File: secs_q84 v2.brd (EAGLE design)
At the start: 97.5 x 69.8 mm, 107 parts, among them IC1 MAX203ECWP, IC2 REF3440TIDBVR, IC3 ADP151AUJZ-3.3-R7, IC5 MCZ33996EK, IC6 74HC125D, IC7 TIC12400DCPR, IC8 PIC18F57Q84-I_PT

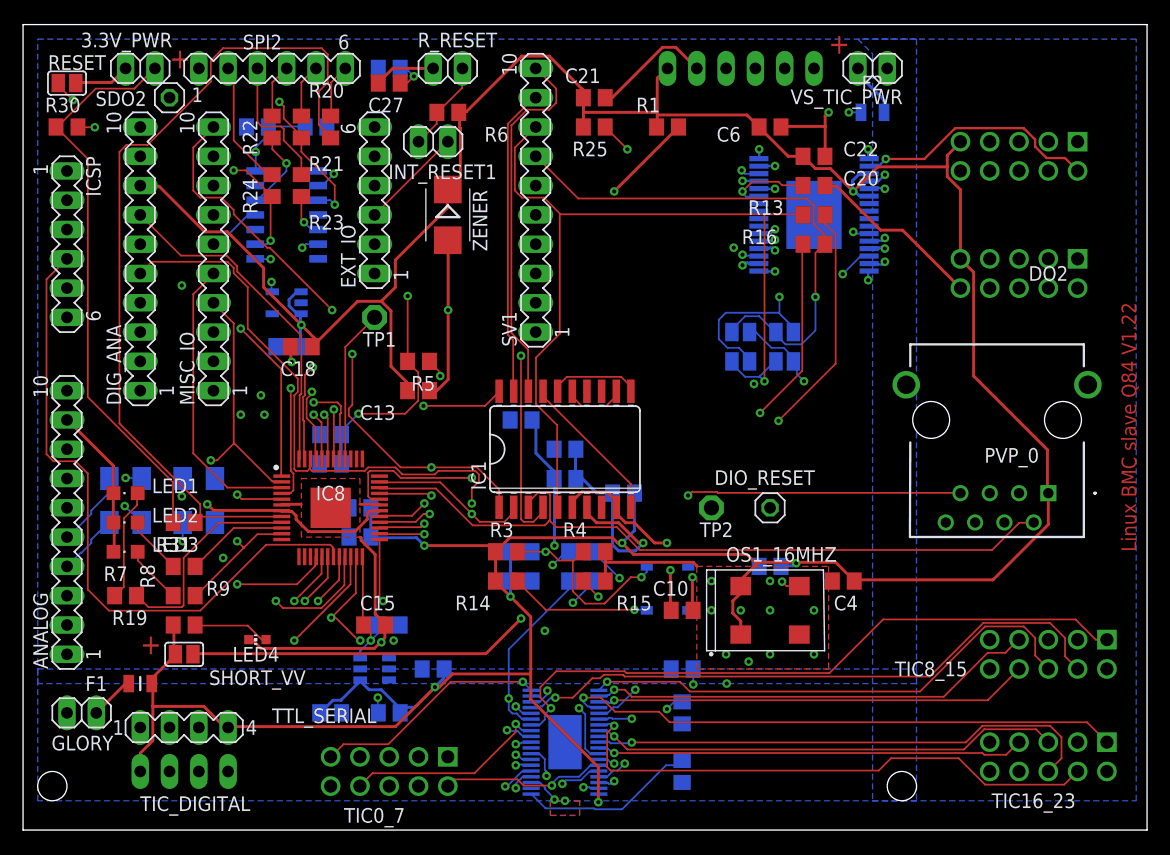
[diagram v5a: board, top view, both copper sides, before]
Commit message: 57Q84 support
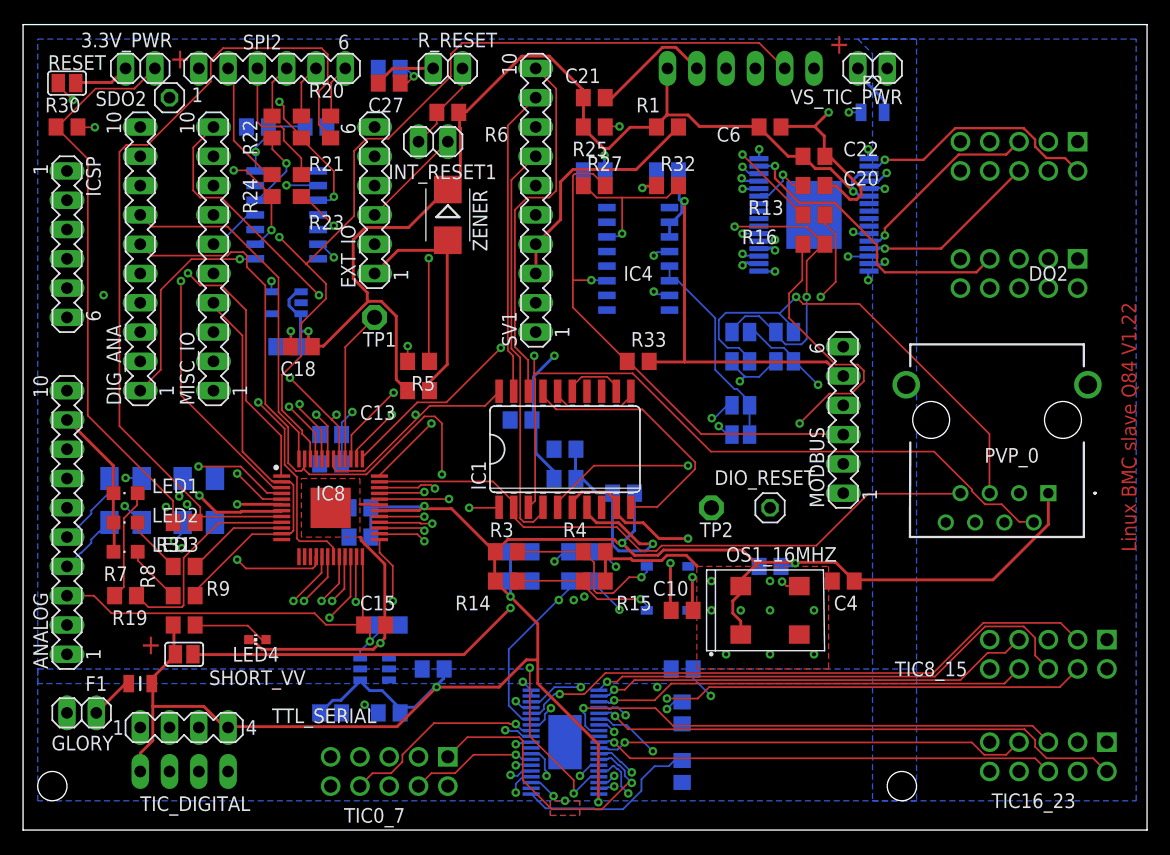
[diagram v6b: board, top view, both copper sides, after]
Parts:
- added C30: 10uf, rcl:C0805
- added C31: 0.1uf, rcl:C0805
- added DE3: DE3, jumper:SJ
- added IC4: ADM3095EBRZ, ADM3095EBRZ:SOIC127P600X175-16N
- added MODBUS: MODBUS, con-lstb:MA06-1
- added R27: 120, rcl:R0805
- added R32, R33: 1.2k, rcl:R0805
- added TXDE3: TXDE3, jumper:SJ
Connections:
- new net DE3: DE3.2, IC8.39, MODBUS.6
- new net DERE: DE3.1, IC4.5, IC4.6, TXDE3.1
- new net MB_A: IC4.11, MODBUS.3, R27.2, R33.1
- new net MB_B: IC4.14, MODBUS.2, R27.1, R32.2
- new net MOD_RX: IC4.7, IC8.36
- new net MOD_TX: IC4.4, IC8.37
- new net TXD3: IC8.38, TXDE3.2
- net VDD: now also C30.1, C31.1, IC4.2, IC4.3, MODBUS.5, R33.2
- net VSS: now also C30.2, C31.2, IC4.1, IC4.10, IC4.12, IC4.13, IC4.15, IC4.16, IC4.8, IC4.9, MODBUS.1, MODBUS.4, R32.1
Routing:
- net DE3: track 0.00 -> 52.3 mm, vias 0 -> 2
- net VDD: track 399.9 -> 448.0 mm, vias 9 -> 11
- net MB_A: track 0.00 -> 45.7 mm, vias 0 -> 1
- net MB_B: track 0.00 -> 41.7 mm, vias 0 -> 1
- net MOD_RX: track 0.00 -> 40.1 mm, vias 0 -> 2
- net TXD3: track 0.00 -> 36.1 mm, vias 0 -> 2
- net SDI1: track 138.8 -> 174.6 mm
- net MOD_TX: track 0.00 -> 34.2 mm, vias 0 -> 2
- net SDO2: track 86.9 -> 58.4 mm, vias 2 -> 3
- net MCZ_CS: track 79.3 -> 107.1 mm, vias 4 -> 2
- net TIC9: track 85.5 -> 65.8 mm, vias 1 -> 2
- net PGC_TICINT: track 110.9 -> 129.3 mm
- net SCK1: track 164.1 -> 145.9 mm, vias 3 -> 5
- net DERE: track 0.00 -> 18.1 mm
- net MB_RX: track 65.3 -> 82.3 mm, vias 0 -> 2
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
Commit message: up
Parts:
- added AUX_IO: AUX_IO, con-lstb:MA06-1
- moved C11 5.68 mm to (53.3, 33.0)
- moved F2 4.02 mm to (94.0, 76.2)
- moved VS_TIC_PWR 3.81 mm to (99.1, 76.2)
- moved C15 2.84 mm to (53.3, 30.5), flipped to the bottom, turned to 180 degrees
- moved C3 2.54 mm to (53.3, 35.6)
- moved DO1 2.54 mm to (115.6, 69.8)
- moved DO2 2.54 mm to (115.6, 59.7)
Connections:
- new net RF4: AUX_IO.3, IC8.12
- new net RF5: AUX_IO.4, IC8.13
- new net RF6: AUX_IO.5, IC8.14
- new net RF7: AUX_IO.6, IC8.15
- net VDD: now also AUX_IO.2
- net VSS: now also AUX_IO.1
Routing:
- net RF6: track 0.00 -> 120.9 mm, vias 0 -> 2
- net RF4: track 0.00 -> 105.2 mm, vias 0 -> 2
- net RF7: track 0.00 -> 103.4 mm, vias 0 -> 2
- net RF5: track 0.00 -> 99.2 mm
- net SDO2: track 58.4 -> 91.5 mm, vias 3 -> 2
- net VDD: track 448.0 -> 478.3 mm
- net SDO1: track 149.1 -> 178.6 mm
- net DIO_RST: track 62.0 -> 89.2 mm
- net SCK1: track 145.9 -> 170.6 mm, vias 5 -> 4
- net VCC: track 72.3 -> 96.6 mm
- net SDI1: track 174.6 -> 151.4 mm
- net CLOCKO: track 45.7 -> 65.2 mm, vias 2 -> 0
- net DE3: track 52.3 -> 68.8 mm
- net MB_RX: track 82.3 -> 66.1 mm
- net MCZ_CS: track 107.1 -> 91.9 mm, vias 2 -> 3
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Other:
- board text added: "Linux BMC slave Q84 V1.223"
- board text removed: "Linux BMC slave Q84 V1.22"

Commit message: up
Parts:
- added C32, C33, C34, C35: 0.1uf, rcl:C0603
- added GLORY_24: GLORY_24, pinhead:1X02
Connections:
- net RF4: now also C35.1
- net RF5: now also C32.1
- net RF6: now also C33.1
- net RF7: now also C34.1
- net VSS: now also C32.2, C33.2, C34.2, C35.2
- net VS_TIC_24V: now also GLORY_24.1, GLORY_24.2
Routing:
- net VS_TIC_24V: track 168.3 -> 176.6 mm
- net RF4: track 105.2 -> 110.9 mm, vias 2 -> 3
- net RF5: track 99.2 -> 103.4 mm
- net RF6: track 120.9 -> 124.2 mm
- net RF7: track 103.4 -> 106.1 mm
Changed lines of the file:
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@@
 <param name="RoutingGrid" value="3mil"/>
 <param name="AutoGrid" value="1"/>
-<param name="Efforts" value="2"/>
+<param name="Efforts" value="1"/>
 <param name="TopRouterVariant" value="1"/>
 <param name="tpViaShape" value="round"/>
@@
 <attribute name="VALUE" x="107.95" y="73.279" size="1.27" layer="27" ratio="10"/>
 </element>
+<element name="GLORY_24" library="pinhead" library_urn="urn:adsk.eagle:library:325" package="1X02" package3d_urn="urn:adsk.eagle:package:22435/2" value="GLORY_24" x="99.06" y="72.39" smashed="yes">
+<attribute name="NAME" x="92.6338" y="69.1388" size="1.27" layer="25" ratio="10"/>
+<attribute name="POPULARITY" value="98" x="99.06" y="72.39" size="1.778" layer="27" display="off"/>
+<attribute name="VALUE" x="96.52" y="69.215" size="1.27" layer="27"/>
+</element>
+<element name="C32" library="rcl" library_urn="urn:adsk.eagle:library:334" package="C0603" package3d_urn="urn:adsk.eagle:package:23616/2" value="0.1uf" x="107.95" y="73.66" smashed="yes" rot="MR0">
+<attribute name="NAME" x="108.585" y="74.295" size="1.27" layer="26" rot="MR0"/>
+<attribute name="POPULARITY" value="37" x="107.95" y="73.66" size="1.778" layer="28" rot="MR0" display="off"/>
+<attribute name="SPICEPREFIX" value="C" x="107.95" y="73.66" size="1.778" layer="28" rot="MR0" display="off"/>
+<attribute name="VALUE" x="108.585" y="71.755" size="1.27" layer="28" rot="MR0"/>
+</element>
+<element name="C33" library="rcl" library_urn="urn:adsk.eagle:library:334" package="C0603" package3d_urn="urn:adsk.eagle:package:23616/2" value="0.1uf" x="111.76" y="73.66" smashed="yes" rot="MR0">
+<attribute name="NAME" x="112.395" y="74.295" size="1.27" layer="26" rot="MR0"/>
+<attribute name="POPULARITY" value="37" x="111.76" y="73.66" size="1.778" layer="28" rot="MR0" display="off"/>
+<attribute name="SPICEPREFIX" value="C" x="111.76" y="73.66" size="1.778" layer="28" rot="MR0" display="off"/>
+<attribute name="VALUE" x="112.395" y="71.755" size="1.27" layer="28" rot="MR0"/>
+</element>
+<element name="C34" library="rcl" library_urn="urn:adsk.eagle:library:334" package="C0603" package3d_urn="urn:adsk.eagle:package:23616/2" value="0.1uf" x="115.57" y="73.66" smashed="yes" rot="MR0">
+<attribute name="NAME" x="116.205" y="74.295" size="1.27" layer="26" rot="MR0"/>
+<attribute name="POPULARITY" value="37" x="115.57" y="73.66" size="1.778" layer="28" rot="MR0" display="off"/>
+<attribute name="SPICEPREFIX" value="C" x="115.57" y="73.66" size="1.778" layer="28" rot="MR0" display="off"/>
+<attribute name="VALUE" x="116.205" y="71.755" size="1.27" layer="28" rot="MR0"/>
+</element>
+<element name="C35" library="rcl" library_urn="urn:adsk.eagle:library:334" package="C0603" package3d_urn="urn:adsk.eagle:package:23616/2" value="0.1uf" x="104.14" y="73.66" smashed="yes" rot="MR0">
+<attribute name="NAME" x="104.775" y="74.295" size="1.27" layer="26" rot="MR0"/>
+<attribute name="POPULARITY" value="37" x="104.14" y="73.66" size="1.778" layer="28" rot="MR0" display="off"/>
+<attribute name="SPICEPREFIX" value="C" x="104.14" y="73.66" size="1.778" layer="28" rot="MR0" display="off"/>
+<attribute name="VALUE" x="104.775" y="71.755" size="1.27" layer="28" rot="MR0"/>
+</element>
 </elements>
 <signals>
@@
 <wire x1="63.5" y1="11.43" x2="63.5" y2="12.7" width="0.254" layer="16"/>
 <wire x1="80.01" y1="28.1178" x2="74.7522" y2="28.1178" width="0.254" layer="1"/>
+<contactref element="C35" pad="2"/>
+<contactref element="C32" pad="2"/>
+<contactref element="C34" pad="2"/>
+<contactref element="C33" pad="2"/>
 </signal>
 <signal name="CPU_CLK">
@@
 <wire x1="94.7928" y1="65.151" x2="94.7928" y2="42.291" width="0.1524" layer="2"/>
 <wire x1="92.0496" y1="67.8942" x2="94.7928" y2="65.151" width="0.1524" layer="2"/>
-<wire x1="92.0496" y1="76.1238" x2="92.0496" y2="67.8942" width="0.1524" layer="2"/>
+<wire x1="92.0496" y1="76.1238" x2="92.0496" y2="72.39" width="0.1524" layer="2"/>
+<wire x1="92.0496" y1="72.39" x2="92.0496" y2="67.8942" width="0.1524" layer="2"/>
 <wire x1="91.9734" y1="76.2" x2="92.0496" y2="76.1238" width="0.1524" layer="2"/>
 <wire x1="105.3846" y1="26.67" x2="105.41" y2="26.67" width="0.1524" layer="2"/>
@@
 <via x="91.9734" y="76.2" extent="1-16" drill="0.35"/>
 <via x="90.6018" y="30.7086" extent="1-16" drill="0.35"/>
+<contactref element="GLORY_24" pad="2"/>
+<contactref element="GLORY_24" pad="1"/>
+<wire x1="100.33" y1="72.39" x2="97.79" y2="72.39" width="0.1524" layer="1"/>
+<wire x1="92.0496" y1="72.39" x2="97.79" y2="72.39" width="0.1524" layer="2"/>
 </signal>
 <signal name="TIC2">
@@
 <wire x1="43.9674" y1="35.2044" x2="44.022" y2="35.35" width="0.1524" layer="1"/>
 <via x="40.1574" y="31.3944" extent="1-16" drill="0.35"/>
+<contactref element="C35" pad="1"/>
+<wire x1="105.0036" y1="74.3712" x2="105.0036" y2="73.6854" width="0.1524" layer="16"/>
+<wire x1="105.3846" y1="74.7522" x2="105.0036" y2="74.3712" width="0.1524" layer="16"/>
+<wire x1="107.7468" y1="74.7522" x2="105.3846" y2="74.7522" width="0.1524" layer="15"/>
+<wire x1="109.1946" y1="76.2" x2="107.7468" y2="74.7522" width="0.1524" layer="15"/>
+<wire x1="105.0036" y1="73.6854" x2="104.99" y2="73.66" width="0.1524" layer="16"/>
+<wire x1="109.1946" y1="76.2" x2="109.22" y2="76.2" width="0.1524" layer="15"/>
+<via x="105.3846" y="74.7522" extent="1-16" drill="0.35"/>
 </signal>
 <signal name="RF7">
@@
 <via x="47.0154" y="26.8986" extent="1-16" drill="0.35"/>
 <via x="82.7532" y="35.2806" extent="1-16" drill="0.35"/>
+<contactref element="C34" pad="1"/>
+<wire x1="116.4336" y1="74.2188" x2="116.4336" y2="73.6854" width="0.1524" layer="16"/>
+<wire x1="116.7384" y1="74.5236" x2="116.4336" y2="74.2188" width="0.1524" layer="16"/>
+<wire x1="116.7384" y1="74.5998" x2="116.7384" y2="74.5236" width="0.1524" layer="16"/>
+<wire x1="116.8146" y1="74.676" x2="116.7384" y2="74.5998" width="0.1524" layer="16"/>
+<wire x1="116.8146" y1="76.2" x2="116.8146" y2="74.676" width="0.1524" layer="16"/>
+<wire x1="116.4336" y1="73.6854" x2="116.42" y2="73.66" width="0.1524" layer="16"/>
+<wire x1="116.8146" y1="76.2" x2="116.84" y2="76.2" width="0.1524" layer="16"/>
 </signal>
 <signal name="RF6">
@@
 <via x="46.101" y="26.8986" extent="1-16" drill="0.35"/>
 <via x="55.0164" y="23.9268" extent="1-16" drill="0.35"/>
+<contactref element="C33" pad="1"/>
+<wire x1="112.6236" y1="74.0664" x2="112.6236" y2="73.6854" width="0.1524" layer="16"/>
+<wire x1="114.3" y1="75.7428" x2="112.6236" y2="74.0664" width="0.1524" layer="16"/>
+<wire x1="114.3" y1="76.2" x2="114.3" y2="75.7428" width="0.1524" layer="16"/>
+<wire x1="112.6236" y1="73.6854" x2="112.61" y2="73.66" width="0.1524" layer="16"/>
 </signal>
 <signal name="RF5">
@@
 <wire x1="45.4914" y1="33.8328" x2="45.51" y2="33.862" width="0.1524" layer="1"/>
 <wire x1="111.7092" y1="76.2" x2="111.76" y2="76.2" width="0.1524" layer="1"/>
+<contactref element="C32" pad="1"/>
+<wire x1="109.5756" y1="73.6854" x2="108.8136" y2="73.6854" width="0.1524" layer="16"/>
+<wire x1="110.109" y1="74.2188" x2="109.5756" y2="73.6854" width="0.1524" layer="16"/>
+<wire x1="110.109" y1="74.295" x2="110.109" y2="74.2188" width="0.1524" layer="16"/>
+<wire x1="111.7092" y1="75.8952" x2="110.109" y2="74.295" width="0.1524" layer="16"/>
+<wire x1="111.7092" y1="76.2" x2="111.7092" y2="75.8952" width="0.1524" layer="16"/>
+<wire x1="108.8136" y1="73.6854" x2="108.8" y2="73.66" width="0.1524" layer="16"/>
+<wire x1="111.7092" y1="76.2" x2="111.76" y2="76.2" width="0.1524" layer="16"/>
 </signal>
 </signals>
